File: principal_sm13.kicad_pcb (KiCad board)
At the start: 2 copper layers, 138.6 x 86.2 mm, 73 parts, among them J1 CN_ARM, J2 CN_POLE, P12 CONN_10X2, P14 SPI, Q1 BC807, Q2 BC807, Q3 BC807, Q4 BC807, U1 AD8397ARZ, U2 AD8397ARZ, U3 L7812, X1 8.192MHz, X2 8.192MHz

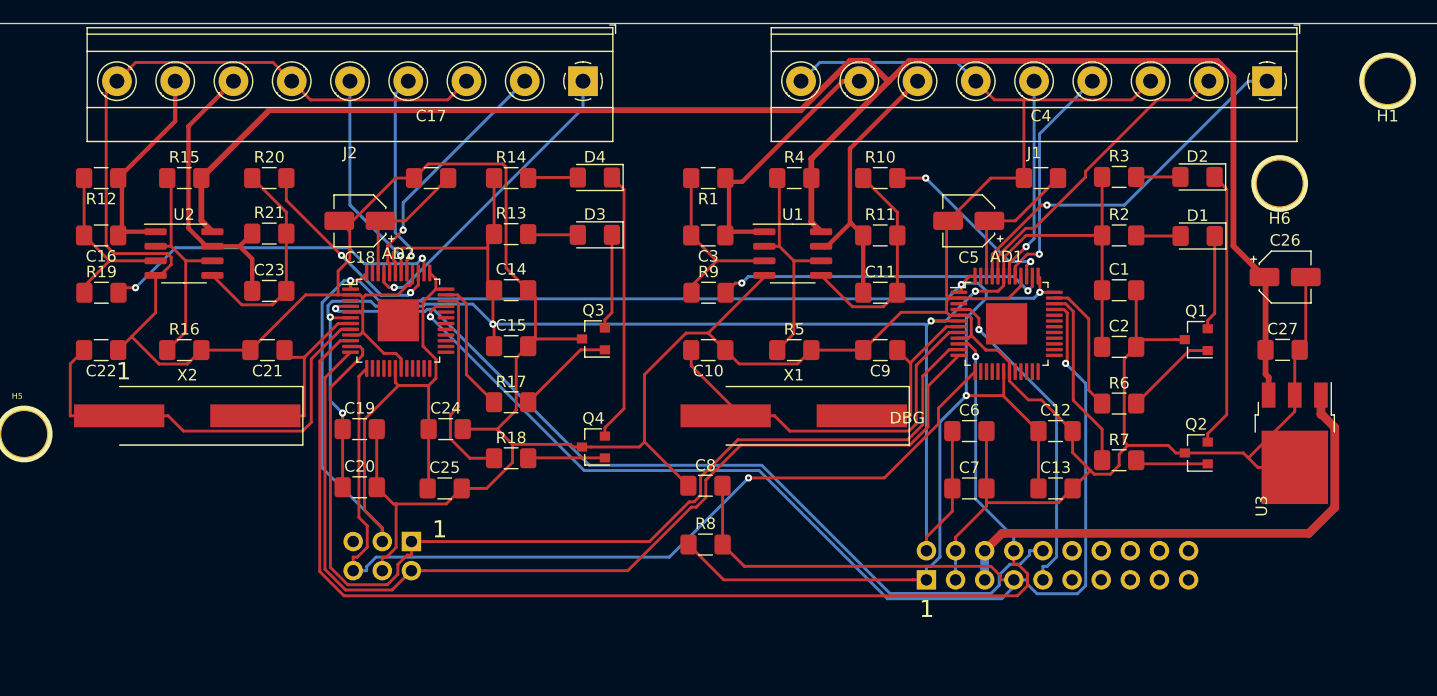
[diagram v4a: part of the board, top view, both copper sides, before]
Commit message: reducida la placa para que queden libres los conectores de la CIAA, ruteado completo, quedan 38 vias
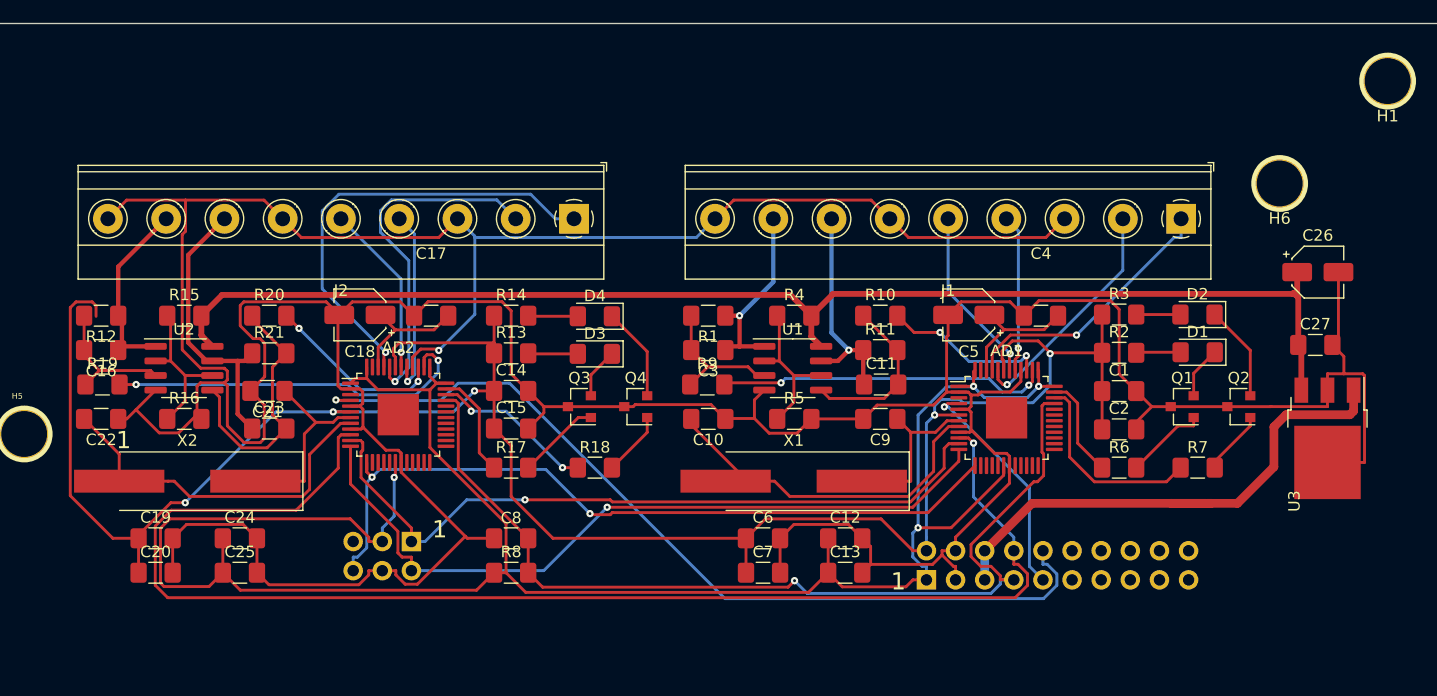
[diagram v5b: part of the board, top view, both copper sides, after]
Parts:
- moved C12 20.6 mm to (234.0, 134.7)
- moved C24 20.3 mm to (181.2, 134.7)
- moved C6 20.3 mm to (226.8, 134.7)
- moved C19 20.2 mm to (173.8, 134.7)
- moved C13 19.8 mm to (234.0, 137.7)
- moved C7 19.4 mm to (226.8, 137.7)
- moved C25 19.3 mm to (181.2, 137.7)
- moved C20 19.3 mm to (173.8, 137.7)
- moved C8 17.5 mm to (204.8, 134.7)
- moved R8 17.1 mm to (204.8, 137.7)
- moved J1 14.2 mm to (263.2, 106.9)
- moved D4 12.1 mm to (212.1, 115.4)
- moved J2 12.0 mm to (210.3, 106.9)
- moved C17 12.0 mm to (197.8, 115.3)
- moved C23 12.0 mm to (183.7, 125.2)
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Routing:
- net /GPIO/GPIO0: track 129.4 -> 84.7 mm, vias 2 -> 1
- net +12V: track 146.6 -> 114.5 mm
- net /RDC ARM/MISO: track 89.9 -> 64.1 mm, vias 0 -> 1
- net +5V: track 165.3 -> 188.2 mm
- net /RDC ARM/MOSI: track 87.3 -> 66.2 mm, vias 0 -> 1
- net GND: track 417.2 -> 438.2 mm, vias 0 -> 1
- net +3V3: track 200.8 -> 183.6 mm
- net Net-(D2-Pad1): track 24.2 -> 8.37 mm
- net Net-(D4-Pad1): track 23.7 -> 8.20 mm
- net /GPIO/SPI_SCK: track 81.4 -> 66.8 mm, vias 1 -> 2
- net /RDC POLE/COS: track 27.2 -> 39.4 mm
- net /GPIO/GPIO1: track 109.0 -> 120.0 mm
- net /RDC POLE/COSLO: track 21.7 -> 30.8 mm
- net /RDC ARM/COS: track 32.1 -> 23.8 mm
- net /GPIO/GPIO2: track 28.4 -> 20.2 mm
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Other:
- board text removed: "DBG"

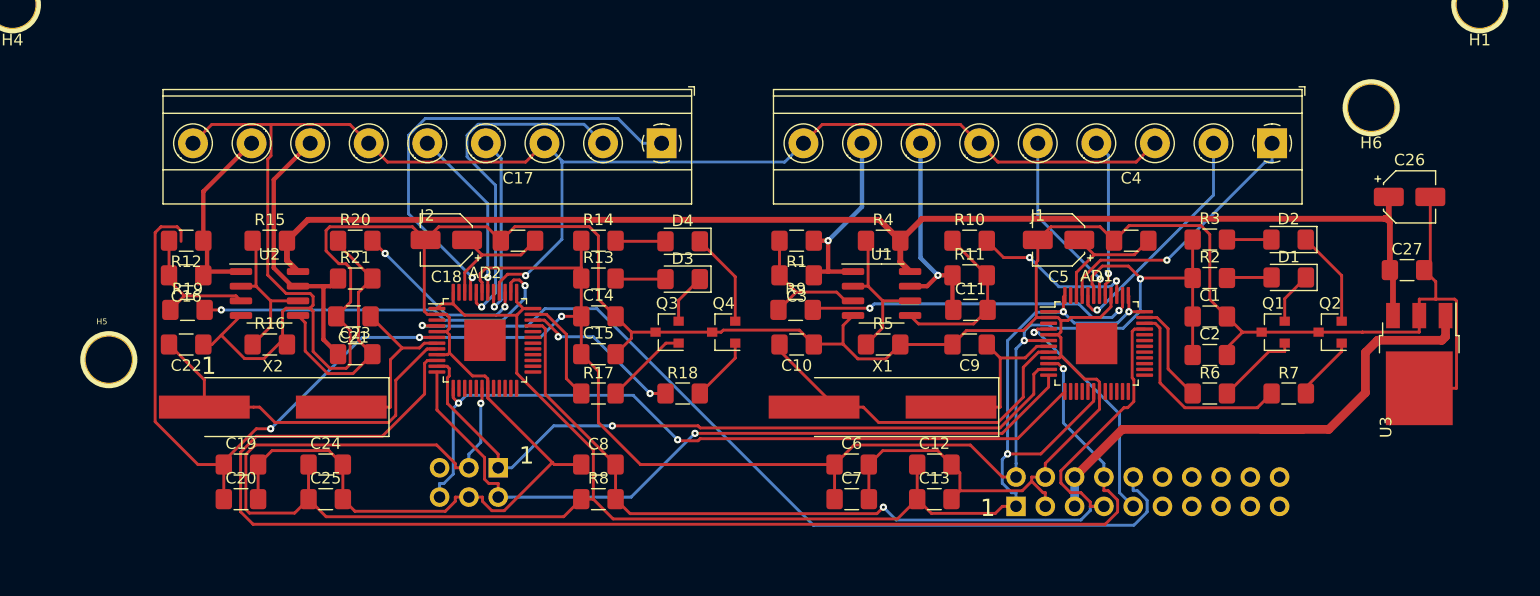
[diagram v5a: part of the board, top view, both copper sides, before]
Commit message: agregadas zonas de relleno conecadas a GND
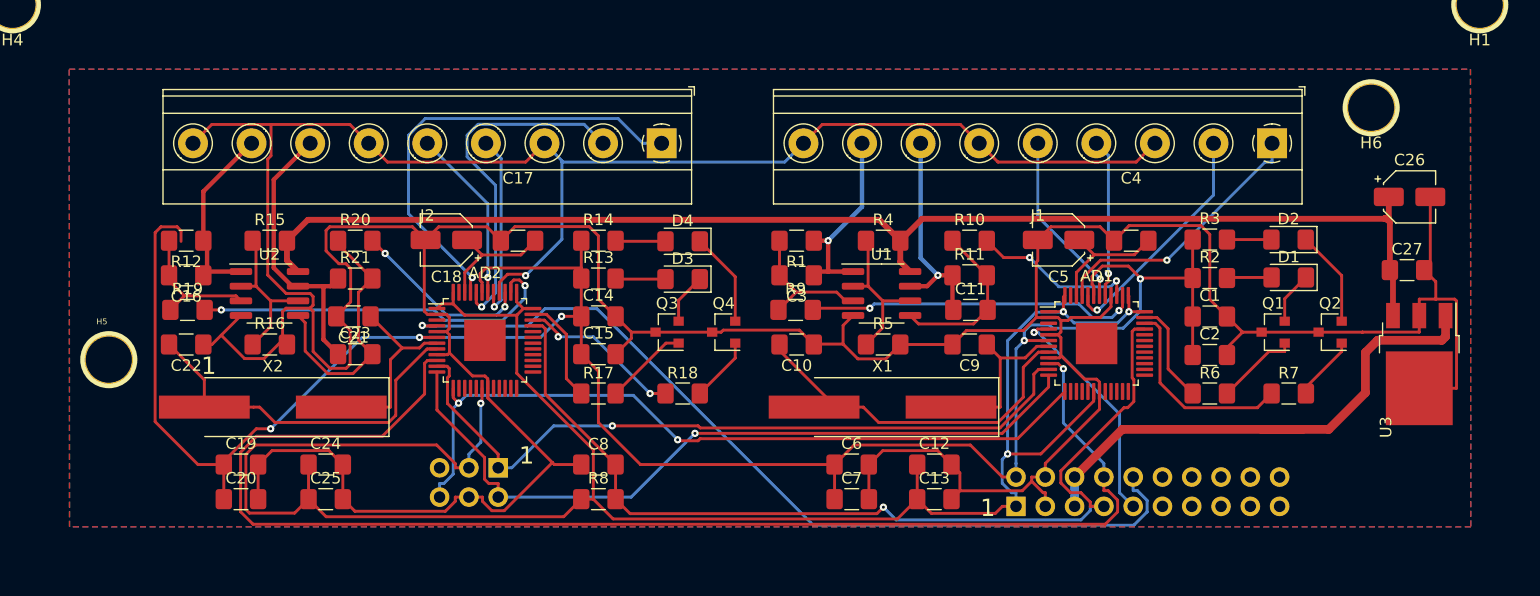
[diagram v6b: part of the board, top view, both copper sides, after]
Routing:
- added copper zone on B.Cu, net GND
- added copper zone on F.Cu, net GND
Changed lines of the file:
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@@
   (general
     (thickness 1.6)
-    (drawings 39)
+    (drawings 40)
     (tracks 727)
     (zones 0)
@@
   (page A3)
   (layers
-    (0 F.Cu mixed)
+    (0 F.Cu mixed hide)
     (31 B.Cu mixed)
     (32 B.Adhes user)
@@
     (pad 1 thru_hole circle (at 0 0 180) (size 4.5 4.5) (drill 4) (layers *.Cu *.Mask F.SilkS))
   )
+  (target plus (at 280.45 140.65) (size 5) (width 0.1) (layer Edge.Cuts))
   (gr_line (start 286.9245 89.8465) (end 286.9245 176.0435) (angle 90) (layer Edge.Cuts) (width 0.1))
   (gr_text 1 (at 198.595 133.958) (layer F.SilkS)
@@
   (segment (start 174.8385 115.325) (end 175.1311 115.6176) (width 0.254) (layer F.Cu) (net 56))
   (segment (start 175.1311 115.6176) (end 175.1311 119.27) (width 0.254) (layer F.Cu) (net 56))
+  (zone (net 2) (net_name GND) (layer F.Cu) (hatch edge 0.508)
+    (connect_pads (clearance 0.508))
+    (min_thickness 0.254)
+    (fill yes (arc_segments 32) (thermal_gap 0.508) (thermal_bridge_width 0.508) (smoothing chamfer) (radius 2))
+    (polygon
+      (pts
+        (xy 280.48 140.14) (xy 158.96 140.14) (xy 158.93 100.45) (xy 280.45 100.45)
+      )
+    )
+  )
+  (zone (net 2) (net_name GND) (layer B.Cu) (hatch edge 0.508)
+    (connect_pads (clearance 0.508))
+    (min_thickness 0.254)
+    (fill yes (arc_segments 32) (thermal_gap 0.508) (thermal_bridge_width 0.508) (smoothing chamfer) (radius 2))
+    (polygon
+      (pts
+        (xy 280.48 140.14) (xy 158.96 140.14) (xy 158.93 100.45) (xy 280.45 100.45)
+      )
+    )
+  )
 )

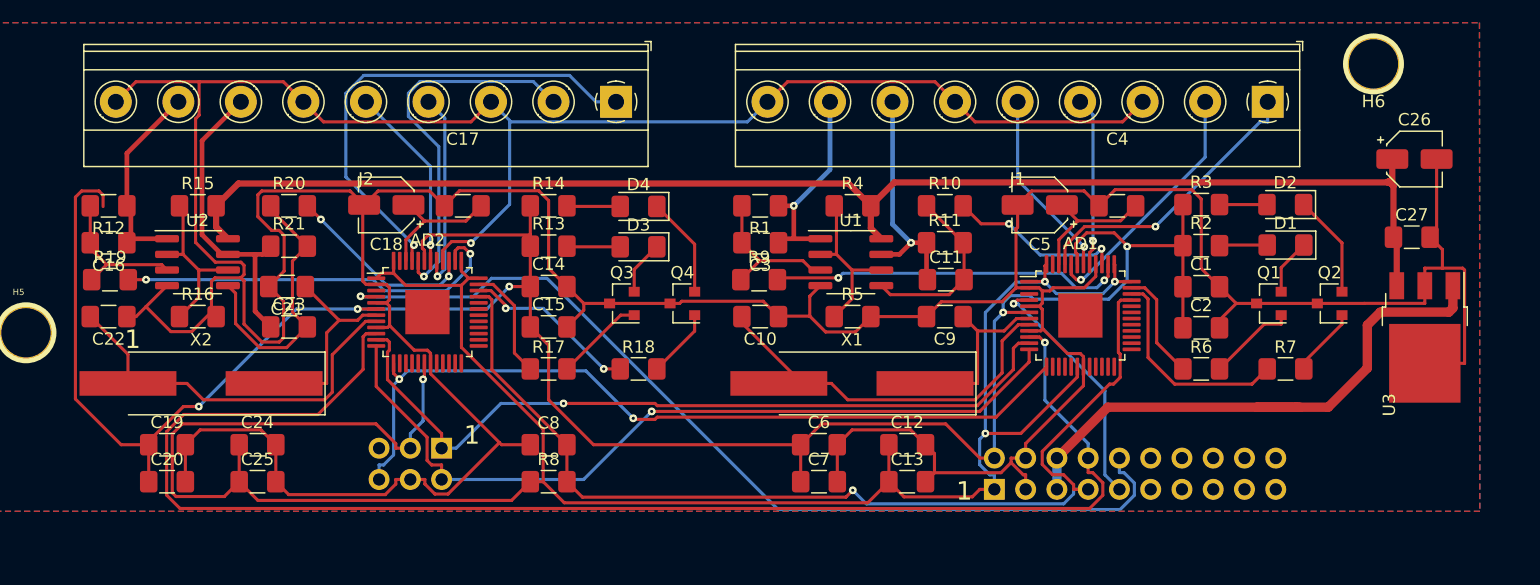
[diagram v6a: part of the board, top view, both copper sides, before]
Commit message: agregados test points parara comunicacion SPI, ruteado, 28 vias
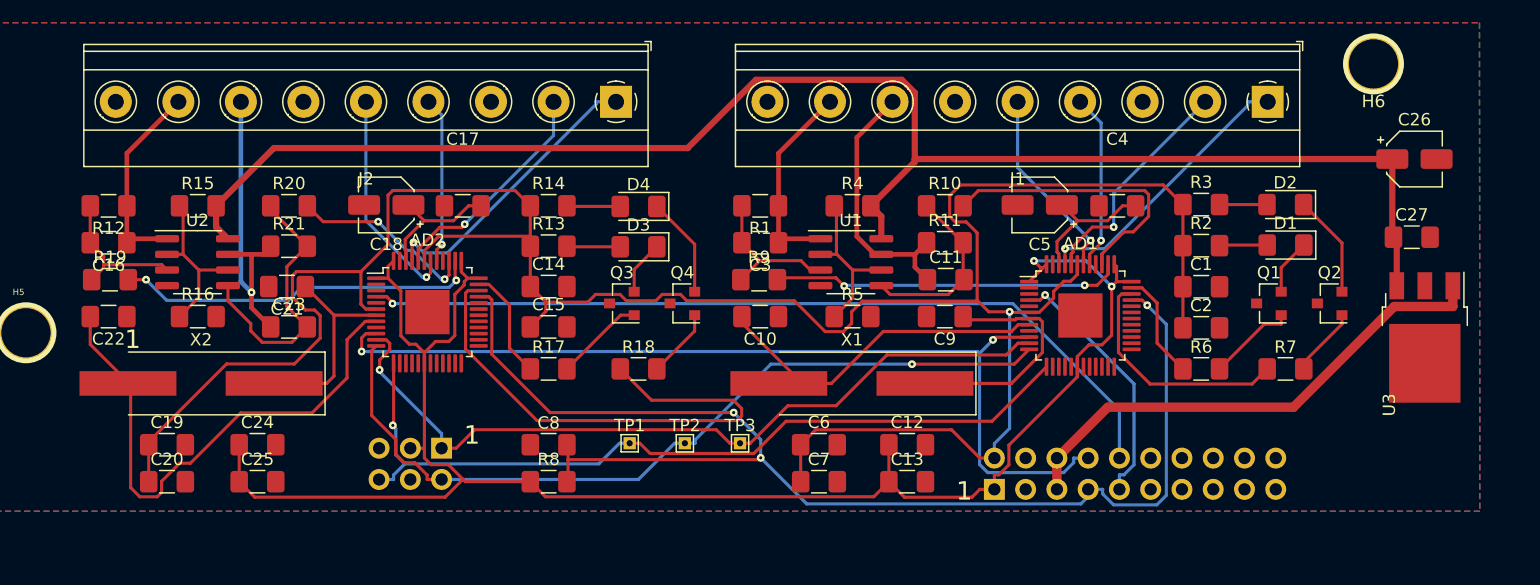
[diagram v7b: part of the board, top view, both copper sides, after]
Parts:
- added TP1: TP_SCK, TestPoint:TestPoint_THTPad_1.0x1.0mm_Drill0.5mm, F.Cu at (211.4, 134.6)
- added TP2: TP_MOSI, TestPoint:TestPoint_THTPad_1.0x1.0mm_Drill0.5mm, F.Cu at (215.9, 134.6)
- added TP3: TP_MISO, TestPoint:TestPoint_THTPad_1.0x1.0mm_Drill0.5mm, F.Cu at (220.4, 134.6)
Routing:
- net GND: track 438.2 -> 0.00 mm, vias 1 -> 0
- net +3V3: track 183.6 -> 139.3 mm, vias 4 -> 2
- net /GPIO/GPIO1: track 120.0 -> 76.1 mm, vias 1 -> 2
- net Net-(AD2-Pad34): track 14.3 -> 42.5 mm, vias 2 -> 0
- net /GPIO/GPIO0: track 84.7 -> 104.8 mm, vias 1 -> 3
- net /RDC POLE/COS: track 39.4 -> 23.6 mm
- net +12V: track 114.5 -> 127.4 mm
- net /RDC POLE/COSLO: track 30.8 -> 18.5 mm
- net Net-(AD2-Pad8): track 31.8 -> 43.9 mm
- net +5V: track 188.2 -> 199.1 mm, vias 5 -> 1
- net /RDC ARM/~EXC: track 14.4 -> 23.4 mm, vias 2 -> 0
- net /GPIO/GPIO3: track 76.8 -> 68.1 mm
- net +24V: track 47.4 -> 41.5 mm
- net Net-(AD1-Pad7): track 14.8 -> 19.8 mm
- net /RDC POLE/SINLO: track 15.1 -> 17.9 mm
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
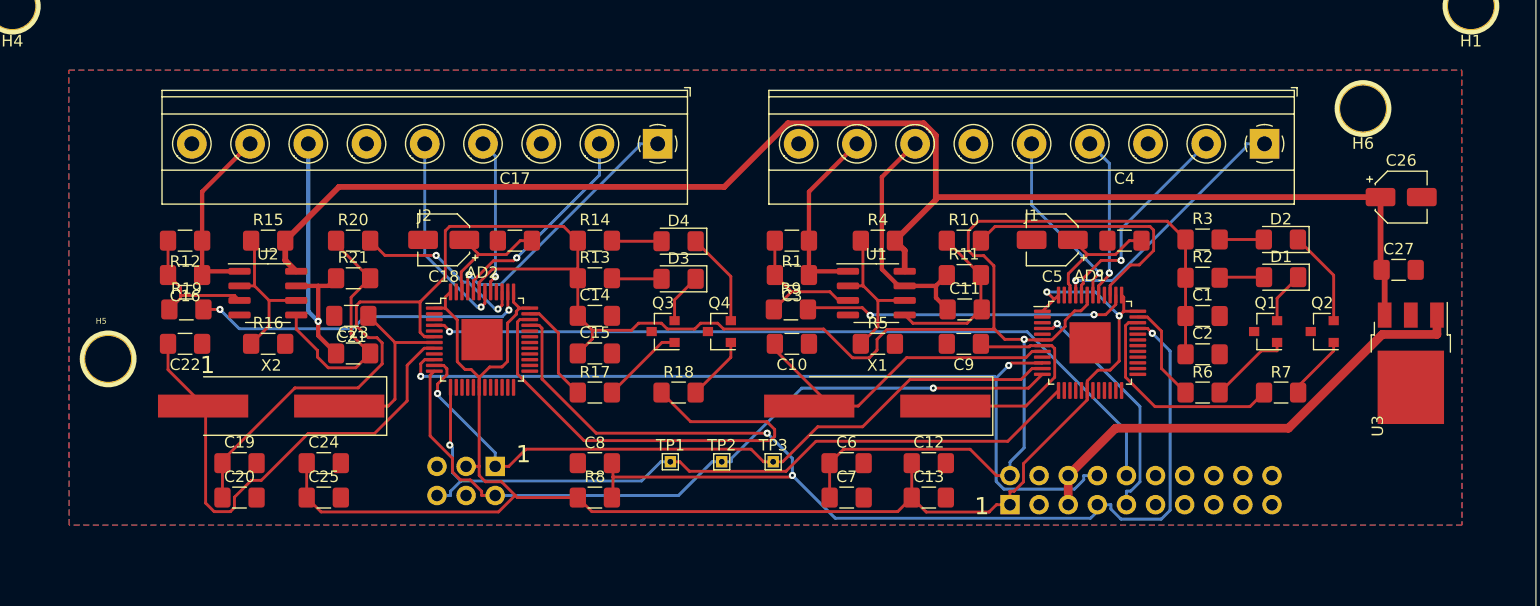
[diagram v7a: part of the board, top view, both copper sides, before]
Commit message: el freerouting no conecta bien si hay zonas llenas, 30 vias
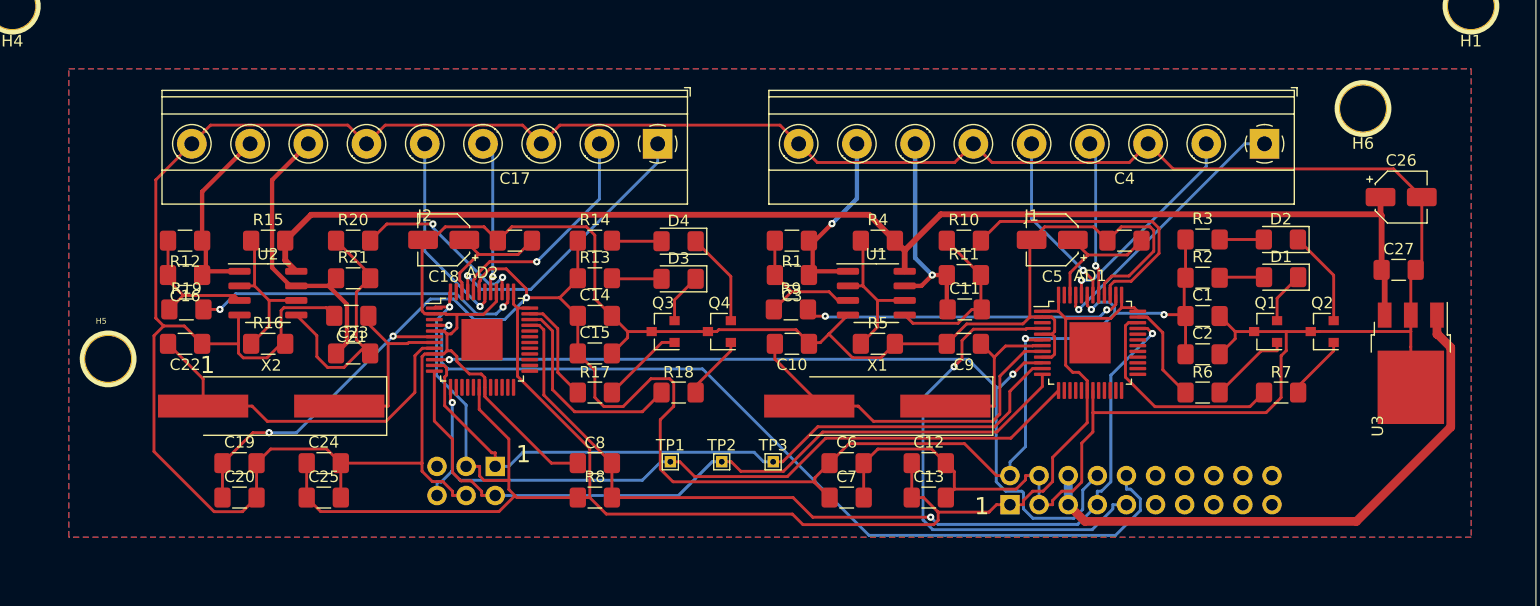
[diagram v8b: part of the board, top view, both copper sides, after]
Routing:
- net GND: track 0.00 -> 456.9 mm
- net +5V: track 199.1 -> 161.5 mm, vias 1 -> 6
- net Net-(AD2-Pad34): track 42.5 -> 18.5 mm
- net /GPIO/GPIO0: track 104.8 -> 81.1 mm, vias 3 -> 2
- net /GPIO/GPIO2: track 20.9 -> 43.7 mm
- net +3V3: track 139.3 -> 161.8 mm, vias 2 -> 1
- net +12V: track 127.4 -> 114.4 mm
- net Net-(AD2-Pad8): track 43.9 -> 31.9 mm
- net +24V: track 41.5 -> 50.2 mm
- net /GPIO/GPIO3: track 68.1 -> 76.6 mm
- net Net-(AD1-Pad7): track 19.8 -> 14.8 mm
- net Net-(AD1-Pad8): track 29.8 -> 32.5 mm
- net Net-(C11-Pad1): track 21.3 -> 19.2 mm, vias 0 -> 1
- net /RDC ARM/~EXC: track 23.4 -> 24.9 mm
- net /RDC POLE/COSLO: track 18.5 -> 19.9 mm
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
